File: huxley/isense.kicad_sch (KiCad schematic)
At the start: 6 parts, among them U3 MAX40201FAUA+

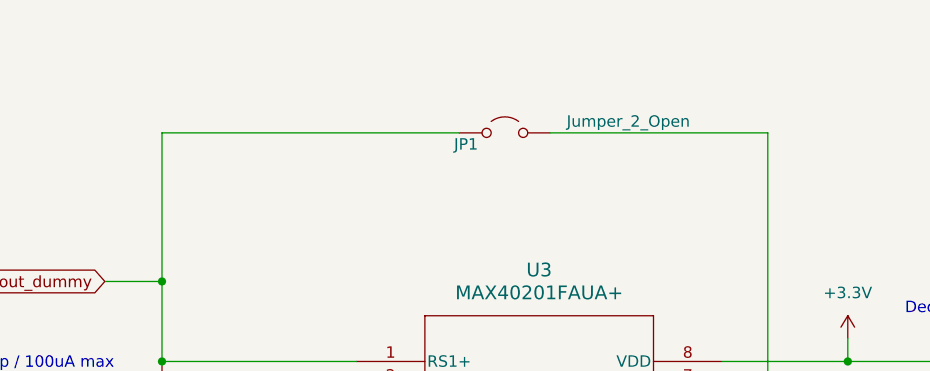
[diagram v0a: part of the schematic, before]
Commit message: updated Ibias gen and footprints
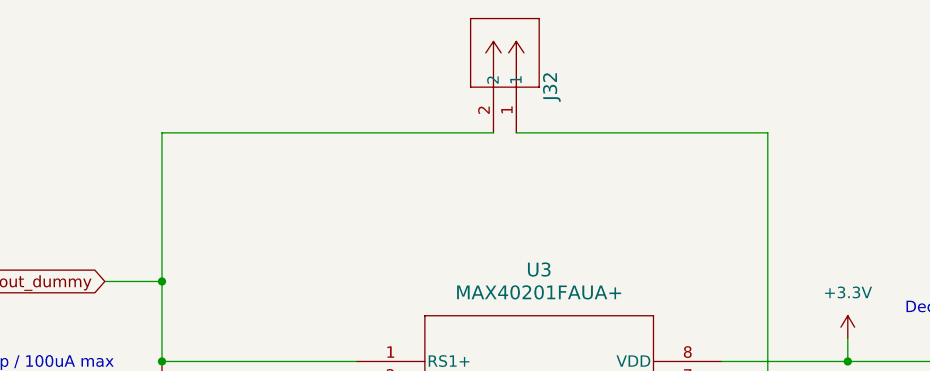
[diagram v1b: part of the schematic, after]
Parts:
- removed JP1: Jumper_2_Open, Jumper:SolderJumper-2_P1.3mm_Open_Pad1.0x1.5mm, symbol Jumper:Jumper_2_Open
- added J32: 61300211121, 726_footprints:CONN_61300211121_WRE, symbol _PHASE:61300211121
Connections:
- net iout_dummy: now also J32.2
- net iout_dummy_amp: now also J32.1
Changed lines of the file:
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@@
-	(wire
-		(pts
-			(xy 142.24 53.34) (xy 166.37 53.34)
-		)
-		(stroke
-			(width 0)
-			(type default)
-		)
-	)
 	(wire
 		(pts
@@
 	(wire
 		(pts
+			(xy 138.43 53.34) (xy 166.37 53.34)
+		)
+		(stroke
+			(width 0)
+			(type default)
+		)
+	)
+	(wire
+		(pts
 			(xy 209.55 77.47) (xy 223.52 77.47)
 		)
@@
 	(wire
 		(pts
-			(xy 132.08 53.34) (xy 99.06 53.34)
+			(xy 99.06 53.34) (xy 135.89 53.34)
 		)
 		(stroke
@@
 	)
 	(symbol
-		(lib_id "Jumper:Jumper_2_Open")
-		(at 137.16 53.34 0)
-		(unit 1)
-		(exclude_from_sim yes)
-		(in_bom yes)
-		(on_board yes)
-		(dnp no)
-		(property "Reference" "JP1"
-			(at 132.842 54.61 0)
-			(effects
-				(font
-					(size 1.27 1.27)
-				)
-			)
-		)
-		(property "Value" "Jumper_2_Open"
-			(at 150.876 52.07 0)
-			(effects
-				(font
-					(size 1.27 1.27)
-				)
-			)
-		)
-		(property "Footprint" "Jumper:SolderJumper-2_P1.3mm_Open_Pad1.0x1.5mm"
-			(at 137.16 53.34 0)
-			(effects
-				(font
-					(size 1.27 1.27)
-				)
-				(hide yes)
-			)
-		)
-		(property "Datasheet" "~"
-			(at 137.16 53.34 0)
-			(effects
-				(font
-					(size 1.27 1.27)
-				)
-				(hide yes)
-			)
-		)
-		(property "Description" "Jumper, 2-pole, open"
-			(at 137.16 53.34 0)
-			(effects
-				(font
-					(size 1.27 1.27)
-				)
-				(hide yes)
-			)
-		)
-		(pin "1"
-		)
-		(pin "2"
-		)
-		(instances
-			(project "huxley"
-				(path "/c6103430-c27a-4e90-8e2e-9404255f5ee3/36719c56-32a6-42e5-970f-52a0fedf7211"
-					(reference "JP1")
-					(unit 1)
-				)
-			)
-		)
-	)
-	(symbol
 		(lib_id "pspice:C")
 		(at 196.85 85.09 0)
@@
 					(unit 1)
 				)
+			)
+		)
+	)
+	(symbol
+		(lib_name "61300211121_1")
+		(lib_id "_PHASE:61300211121")
+		(at 138.43 53.34 270)
+		(mirror x)
+		(unit 1)
+		(exclude_from_sim no)
+		(in_bom yes)
+		(on_board yes)
+		(dnp no)
+		(property "Reference" "J32"
+			(at 142.24 49.784 0)
+			(effects
+				(font
+					(size 1.524 1.524)
+				)
+				(justify left)
+			)
+		)
+		(property "Value" "61300211121"
+			(at 135.8901 39.37 0)
+			(effects
+				(font
+					(size 1.524 1.524)
+				)
+				(justify left)
+				(hide yes)
+			)
+		)
+		(property "Footprint" "726_footprints:CONN_61300211121_WRE"
+			(at 138.43 53.34 0)
+			(effects
+				(font
+					(size 1.27 1.27)
+					(italic yes)
+				)
+				(hide yes)
+			)
+		)
+		(property "Datasheet" "61300211121"
+			(at 138.43 53.34 0)
+			(effects
+				(font
+					(size 1.27 1.27)
+					(italic yes)
+				)
+				(hide yes)
+			)
+		)
+		(property "Description" ""
+			(at 138.43 53.34 0)
+			(effects
+				(font
+					(size 1.27 1.27)
+				)
+				(hide yes)
+			)
+		)
+		(pin "1"
+		)
+		(pin "2"
+		)
+		(instances
+			(project "huxley"
+				(path "/c6103430-c27a-4e90-8e2e-9404255f5ee3/36719c56-32a6-42e5-970f-52a0fedf7211"
+					(reference "J32")
+					(unit 1)
+				)

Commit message: layout_1003
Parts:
- C13, C14, C15: footprint Capacitor_SMD:C_0402_1005Metric -> Capacitor_SMD:C_0603_1608Metric
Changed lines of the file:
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@@
 			)
 		)
-		(property "Footprint" "Capacitor_SMD:C_0402_1005Metric"
+		(property "Footprint" "Capacitor_SMD:C_0603_1608Metric"
 			(at 223.52 83.82 0)
 			(effects
@@
 			)
 		)
-		(property "Footprint" "Capacitor_SMD:C_0402_1005Metric"
+		(property "Footprint" "Capacitor_SMD:C_0603_1608Metric"
 			(at 196.85 85.09 0)
 			(effects
@@
 			)
 		)
-		(property "Footprint" "Capacitor_SMD:C_0402_1005Metric"
+		(property "Footprint" "Capacitor_SMD:C_0603_1608Metric"
 			(at 209.55 85.09 0)
 			(effects

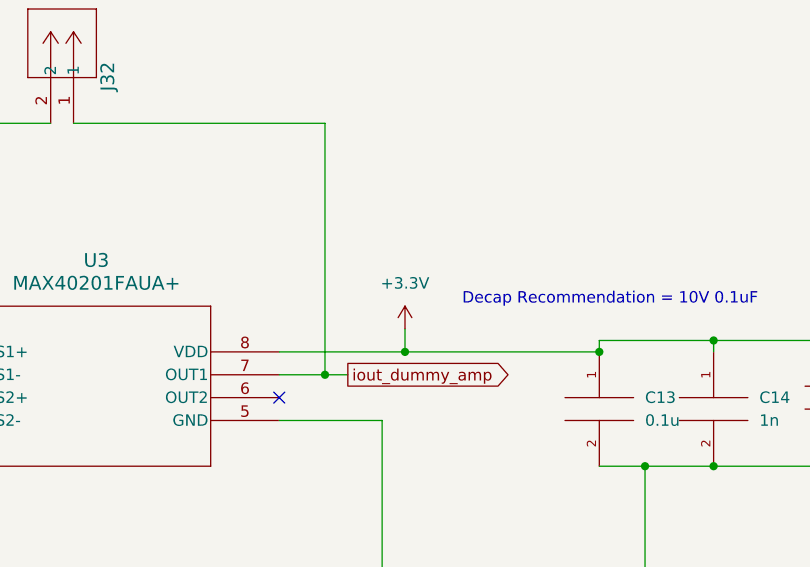
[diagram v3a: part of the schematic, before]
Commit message: reorganized pin assignment to level shifter; matched 3V3 power net name; minor schematic cleanup
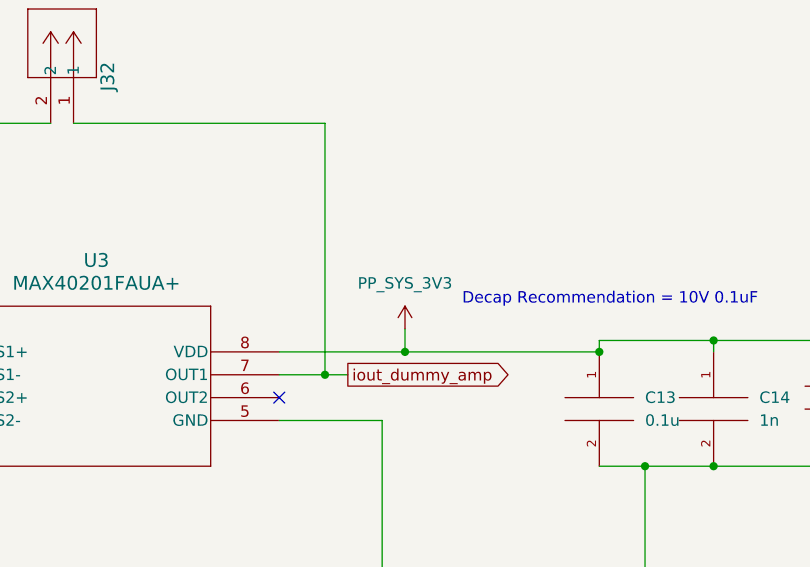
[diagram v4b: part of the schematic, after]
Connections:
- net +3.3V renamed PP_SYS_3V3
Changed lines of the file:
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@@
 			)
 		)
-		(property "Value" "+3.3V"
+		(property "Value" "PP_SYS_3V3"
 			(at 175.26 71.12 0)
 			(effects

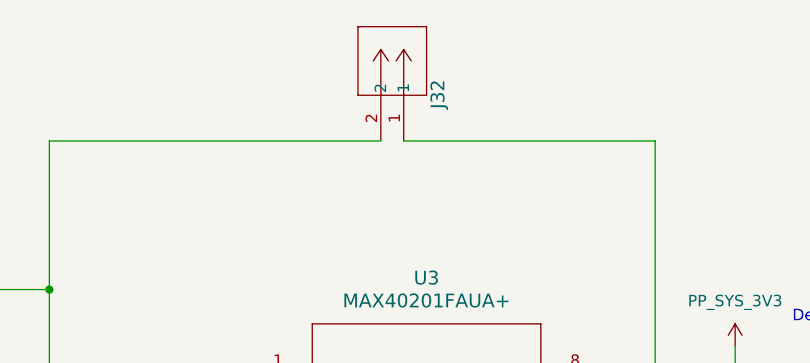
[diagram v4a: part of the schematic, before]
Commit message: fixed all bad refs; replaced analog discovery connector; change level shifter 3v3 to from analog discovery
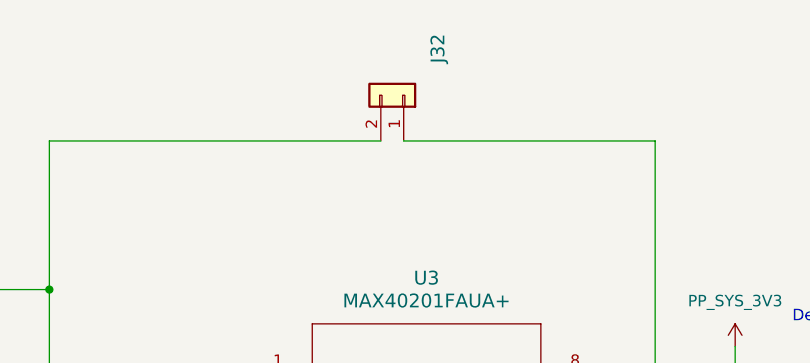
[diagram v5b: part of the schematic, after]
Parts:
- J32: footprint 726_footprints:CONN_61300211121_WRE -> Connector_PinHeader_2.54mm:PinHeader_1x02_P2.54mm_Vertical; symbol _PHASE:61300211121 -> Connector_Generic:Conn_01x02
- U3: footprint 726_footprints:MAX40201FAUA+ -> 0_726_footprints:MAX40201FAUA+; symbol _PHASE:MAX40201FAUA+ -> 0_PHASE:MAX40201FAUA+
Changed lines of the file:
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@@
 	)
 	(symbol
-		(lib_id "_PHASE:MAX40201FAUA+")
+		(lib_id "0_PHASE:MAX40201FAUA+")
 		(at 120.65 78.74 0)
 		(unit 1)
@@
 			)
 		)
-		(property "Footprint" "726_footprints:MAX40201FAUA+"
+		(property "Footprint" "0_726_footprints:MAX40201FAUA+"
 			(at 120.65 78.74 0)
 			(effects
@@
 	)
 	(symbol
-		(lib_id "_PHASE:61300211121")
-		(at 138.43 53.34 270)
+		(lib_id "Connector_Generic:Conn_01x02")
+		(at 138.43 48.26 270)
 		(mirror x)
 		(unit 1)
@@
 		(dnp no)
 		(property "Reference" "J32"
-			(at 142.24 49.784 0)
+			(at 142.24 44.704 0)
 			(effects
 				(font
@@
 		)
 		(property "Value" "61300211121"
-			(at 135.8901 39.37 0)
+			(at 135.8901 34.29 0)
 			(effects
 				(font
@@
 			)
 		)
-		(property "Footprint" "726_footprints:CONN_61300211121_WRE"
-			(at 138.43 53.34 0)
+		(property "Footprint" "Connector_PinHeader_2.54mm:PinHeader_1x02_P2.54mm_Vertical"
+			(at 138.43 48.26 0)
 			(effects
 				(font
 					(size 1.27 1.27)
-					(italic yes)
 				)
 				(hide yes)
 			)
 		)
-		(property "Datasheet" "61300211121"
-			(at 138.43 53.34 0)
+		(property "Datasheet" "~"
+			(at 138.43 48.26 0)
 			(effects
 				(font
 					(size 1.27 1.27)
-					(italic yes)
 				)
 				(hide yes)
 			)
 		)
-		(property "Description" ""
-			(at 138.43 53.34 0)
+		(property "Description" "Generic connector, single row, 01x02, script generated (kicad-library-utils/schlib/autogen/connector/)"
+			(at 138.43 48.26 0)
 			(effects
 				(font

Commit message: layout_1010
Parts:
- C13, C14, C15: symbol pspice:C -> Device:C_Small

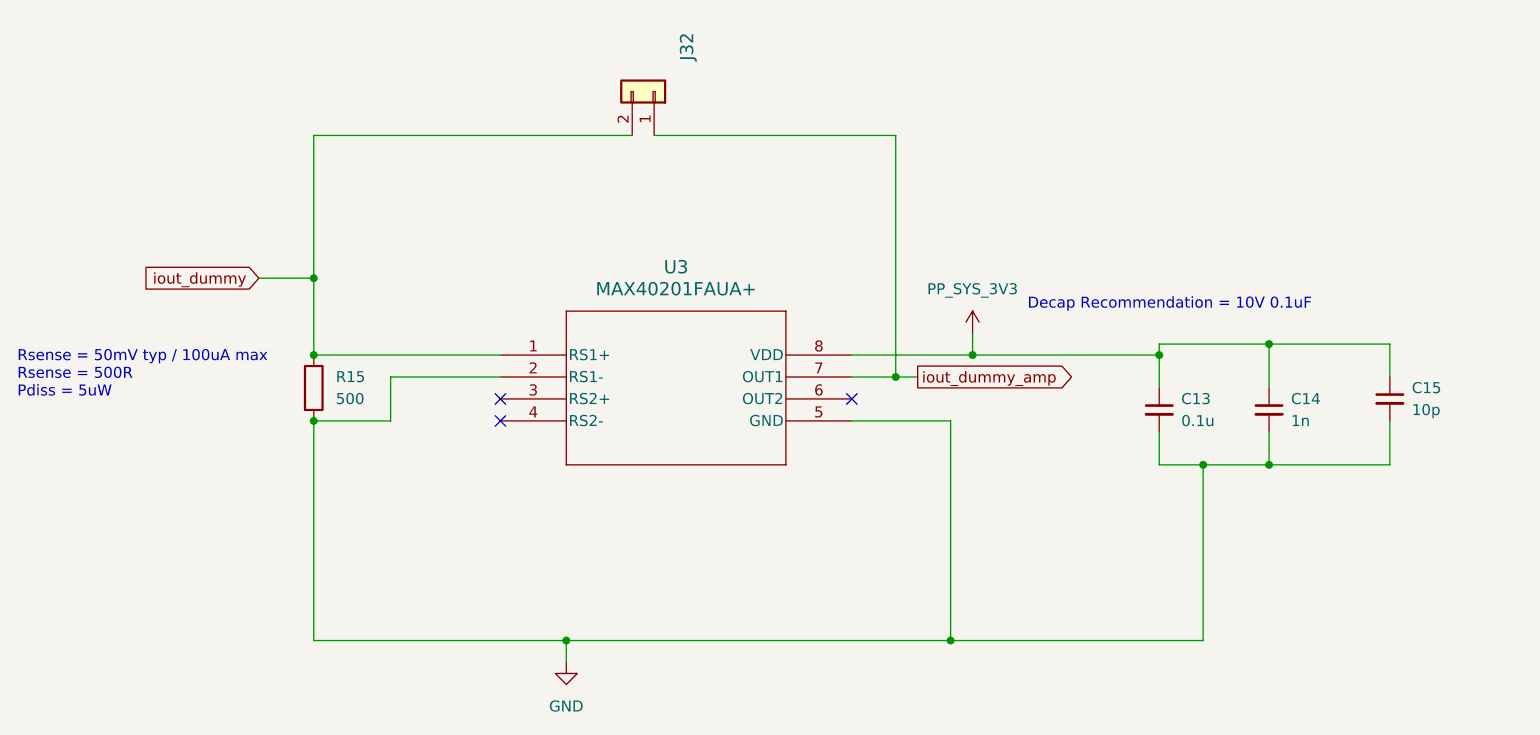
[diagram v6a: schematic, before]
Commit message: minor schematic cleanup; addition of mounting holes; minor layout adjustment
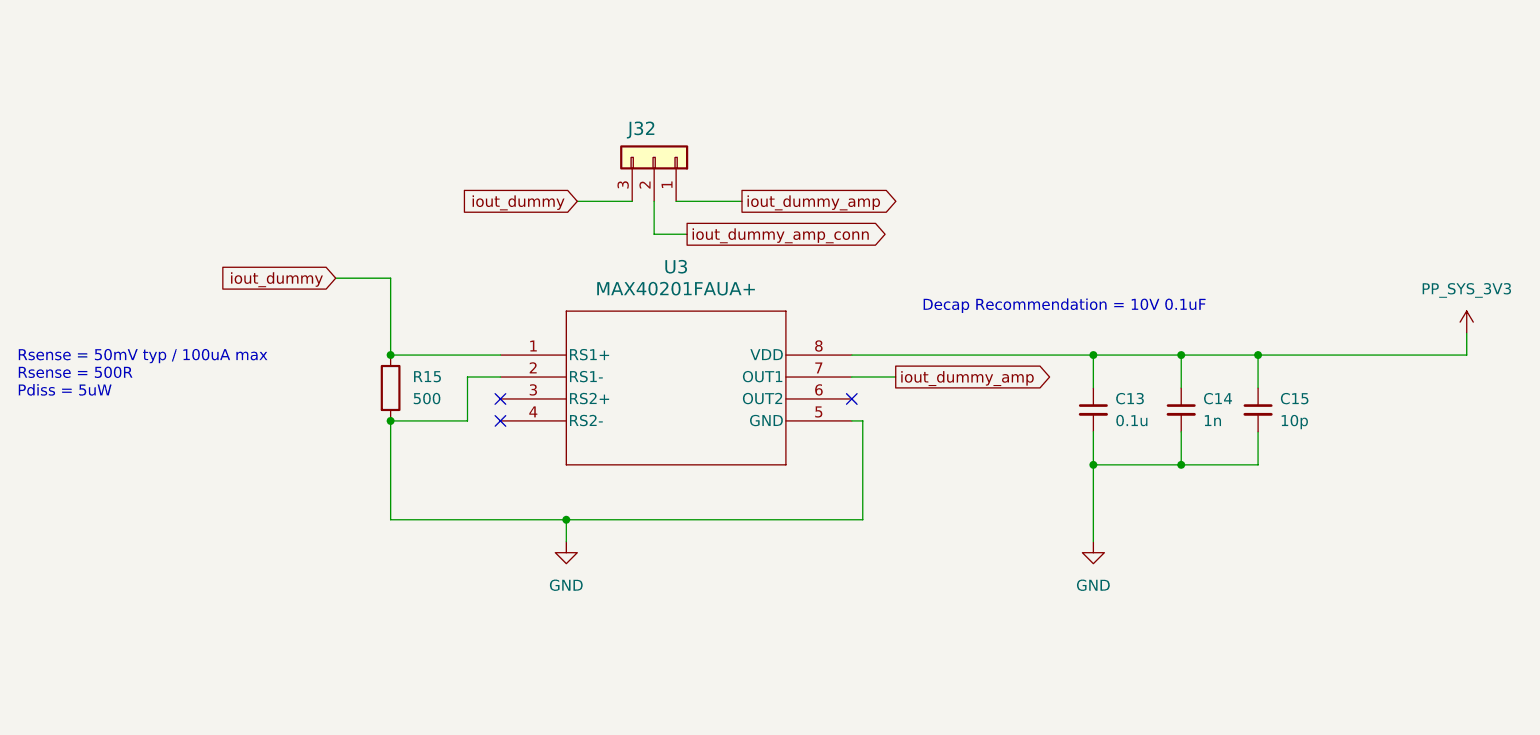
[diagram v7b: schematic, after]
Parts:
- J32: footprint Connector_PinHeader_2.54mm:PinHeader_1x02_P2.54mm_Vertical -> Connector_PinHeader_2.54mm:PinHeader_1x03_P2.54mm_Vertical; symbol Connector_Generic:Conn_01x02 -> Connector_Generic:Conn_01x03
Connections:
- net iout_dummy: now also J32.3 (Pin_3); no longer J32.2 (Pin_2)
- new net iout_dummy_amp_conn: J32.2 (Pin_2)
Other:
- moved on the sheet: C13, C14, C15, R15

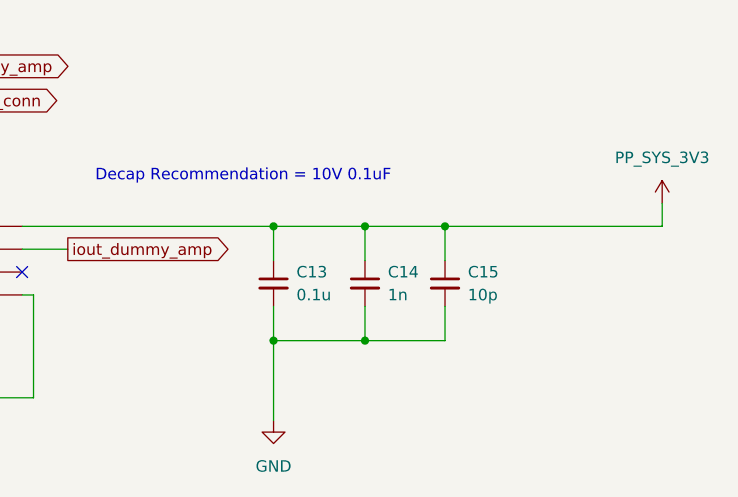
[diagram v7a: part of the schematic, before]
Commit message: added DNP prop to some caps and updated bom; added regular and rounded board outputs
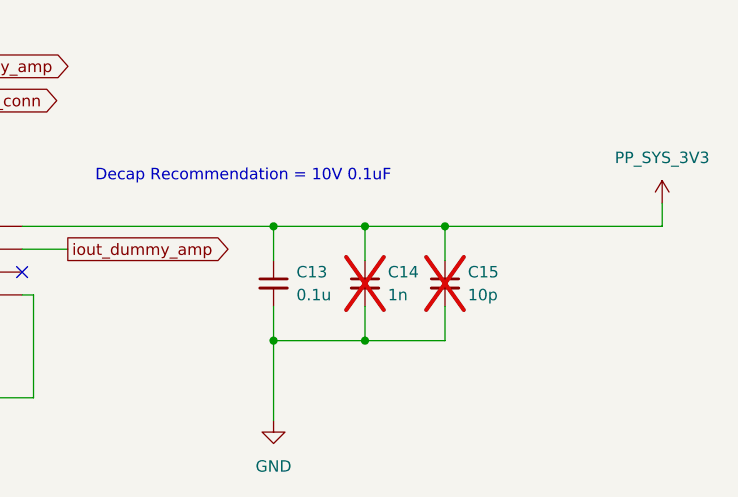
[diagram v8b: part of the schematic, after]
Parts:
- C14, C15: now not fitted
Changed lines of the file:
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@@
 		(in_bom yes)
 		(on_board yes)
-		(dnp no)
+		(dnp yes)
 		(fields_autoplaced yes)
 		(property "Reference" "C15"
@@
 		(in_bom yes)
 		(on_board yes)
-		(dnp no)
+		(dnp yes)
 		(fields_autoplaced yes)
 		(property "Reference" "C14"
